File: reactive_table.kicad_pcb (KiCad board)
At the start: 4 copper layers, 111.8 x 116.8 mm, 184 parts, among them J1 BOT, J2 LEFT, J3 PROGRAM, J4 PWR_LEFT, J5 RIGHT, J6 PWR_RIGHT, J7 PWR_BOT, J8 TOP, J9 PWR_TOP, U1 uA7805, U2 CY8C4124PVI-432, U3 STP08DP05, U4 STP08DP05, U5 TLC274, U6 TLC274, U7 TLC274, U8 TLC274

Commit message: Reworked schematic. Started board
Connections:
- D23 pad 16: /LED Drivers & MUXs/IR15 -> /MUX_IN15
- D23 pad 17: /LED Drivers & MUXs/IR14 -> /MUX_IN14
- D23 pad 18: /LED Drivers & MUXs/IR13 -> /MUX_IN13
- D23 pad 19: /LED Drivers & MUXs/IR12 -> /MUX_IN12
- D23 pad 2: /LED Drivers & MUXs/IR7 -> /MUX_IN7
- D23 pad 20: /LED Drivers & MUXs/IR11 -> /MUX_IN11
- D23 pad 21: /LED Drivers & MUXs/IR10 -> /MUX_IN10
- D23 pad 22: /LED Drivers & MUXs/IR9 -> /MUX_IN9
- D23 pad 23: /LED Drivers & MUXs/IR8 -> /MUX_IN8
- D23 pad 3: /LED Drivers & MUXs/IR6 -> /MUX_IN6
- D23 pad 4: /LED Drivers & MUXs/IR5 -> /MUX_IN5
- D23 pad 5: /LED Drivers & MUXs/IR4 -> /MUX_IN4
- D23 pad 6: /LED Drivers & MUXs/IR3 -> /MUX_IN3
- D23 pad 7: /LED Drivers & MUXs/IR2 -> /MUX_IN2
- D23 pad 8: /LED Drivers & MUXs/IR1 -> /MUX_IN1
- D23 pad 9: /LED Drivers & MUXs/IR0 -> /MUX_IN0
- R1 pad 1: /Microcontroller/BOARD0 -> Net-(D23-Pad1)
- R1 pad 2: Net-(D23-Pad1) -> /Microcontroller/BOARD0
- R2 pad 1: GND -> /Microcontroller/BOARD0
- R2 pad 2: /Microcontroller/BOARD0 -> GND
- R51 pad 2: Net-(R51-Pad2) -> /LED Drivers & MUXs/IR0
- R52 pad 2: Net-(R52-Pad2) -> /LED Drivers & MUXs/IR1
- R53 pad 2: Net-(R53-Pad2) -> /LED Drivers & MUXs/IR2
- R54 pad 2: Net-(R54-Pad2) -> /LED Drivers & MUXs/IR3
- R55 pad 2: Net-(R55-Pad2) -> /LED Drivers & MUXs/IR4
- R56 pad 2: Net-(R56-Pad2) -> /LED Drivers & MUXs/IR5
- R57 pad 2: Net-(R57-Pad2) -> /LED Drivers & MUXs/IR6
- R58 pad 2: Net-(R58-Pad2) -> /LED Drivers & MUXs/IR7
- R59 pad 2: Net-(R59-Pad2) -> /LED Drivers & MUXs/IR8
- R60 pad 2: Net-(R60-Pad2) -> /LED Drivers & MUXs/IR9
- R61 pad 2: Net-(R61-Pad2) -> /LED Drivers & MUXs/IR10
- R62 pad 2: Net-(R62-Pad2) -> /LED Drivers & MUXs/IR11
- R63 pad 2: Net-(R63-Pad2) -> /LED Drivers & MUXs/IR12
- R64 pad 2: Net-(R64-Pad2) -> /LED Drivers & MUXs/IR13
- R65 pad 2: Net-(R65-Pad2) -> /LED Drivers & MUXs/IR14
- R66 pad 2: Net-(R66-Pad2) -> /LED Drivers & MUXs/IR15
- U5 pad 1: /LED Drivers & MUXs/IR0 -> /MUX_IN0
- U5 pad 10: Net-(R53-Pad2) -> /LED Drivers & MUXs/IR2
- U5 pad 12: Net-(R54-Pad2) -> /LED Drivers & MUXs/IR3
- U5 pad 13: /LED Drivers & MUXs/IR3 -> /MUX_IN3
- U5 pad 14: /LED Drivers & MUXs/IR3 -> /MUX_IN3
- U5 pad 2: /LED Drivers & MUXs/IR0 -> /MUX_IN0
- U5 pad 3: Net-(R51-Pad2) -> /LED Drivers & MUXs/IR0
- U5 pad 5: Net-(R52-Pad2) -> /LED Drivers & MUXs/IR1
- U5 pad 6: /LED Drivers & MUXs/IR1 -> /MUX_IN1
- U5 pad 7: /LED Drivers & MUXs/IR1 -> /MUX_IN1
- U5 pad 8: /LED Drivers & MUXs/IR2 -> /MUX_IN2
- U5 pad 9: /LED Drivers & MUXs/IR2 -> /MUX_IN2
- U6 pad 1: /LED Drivers & MUXs/IR4 -> /MUX_IN4
- U6 pad 10: Net-(R57-Pad2) -> /LED Drivers & MUXs/IR6
- U6 pad 12: Net-(R58-Pad2) -> /LED Drivers & MUXs/IR7
- U6 pad 13: /LED Drivers & MUXs/IR7 -> /MUX_IN7
- U6 pad 14: /LED Drivers & MUXs/IR7 -> /MUX_IN7
- U6 pad 2: /LED Drivers & MUXs/IR4 -> /MUX_IN4
- U6 pad 3: Net-(R55-Pad2) -> /LED Drivers & MUXs/IR4
- U6 pad 5: Net-(R56-Pad2) -> /LED Drivers & MUXs/IR5
- U6 pad 6: /LED Drivers & MUXs/IR5 -> /MUX_IN5
- U6 pad 7: /LED Drivers & MUXs/IR5 -> /MUX_IN5
- U6 pad 8: /LED Drivers & MUXs/IR6 -> /MUX_IN6
- U6 pad 9: /LED Drivers & MUXs/IR6 -> /MUX_IN6
- U7 pad 1: /LED Drivers & MUXs/IR8 -> /MUX_IN8
- U7 pad 10: Net-(R61-Pad2) -> /LED Drivers & MUXs/IR10
- U7 pad 12: Net-(R62-Pad2) -> /LED Drivers & MUXs/IR11
- U7 pad 13: /LED Drivers & MUXs/IR11 -> /MUX_IN11
- U7 pad 14: /LED Drivers & MUXs/IR11 -> /MUX_IN11
- U7 pad 2: /LED Drivers & MUXs/IR8 -> /MUX_IN8
- U7 pad 3: Net-(R59-Pad2) -> /LED Drivers & MUXs/IR8
- U7 pad 5: Net-(R60-Pad2) -> /LED Drivers & MUXs/IR9
- U7 pad 6: /LED Drivers & MUXs/IR9 -> /MUX_IN9
- U7 pad 7: /LED Drivers & MUXs/IR9 -> /MUX_IN9
- U7 pad 8: /LED Drivers & MUXs/IR10 -> /MUX_IN10
- U7 pad 9: /LED Drivers & MUXs/IR10 -> /MUX_IN10
- U8 pad 1: /LED Drivers & MUXs/IR12 -> /MUX_IN12
- U8 pad 10: Net-(R65-Pad2) -> /LED Drivers & MUXs/IR14
- U8 pad 12: Net-(R66-Pad2) -> /LED Drivers & MUXs/IR15
- U8 pad 13: /LED Drivers & MUXs/IR15 -> /MUX_IN15
- U8 pad 14: /LED Drivers & MUXs/IR15 -> /MUX_IN15
- U8 pad 2: /LED Drivers & MUXs/IR12 -> /MUX_IN12
- U8 pad 3: Net-(R63-Pad2) -> /LED Drivers & MUXs/IR12
- U8 pad 5: Net-(R64-Pad2) -> /LED Drivers & MUXs/IR13
- U8 pad 6: /LED Drivers & MUXs/IR13 -> /MUX_IN13
- U8 pad 7: /LED Drivers & MUXs/IR13 -> /MUX_IN13
- U8 pad 8: /LED Drivers & MUXs/IR14 -> /MUX_IN14
- U8 pad 9: /LED Drivers & MUXs/IR14 -> /MUX_IN14
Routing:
- net /BRD5: track 338.3 -> 0.00 mm, vias 1 -> 0
- net /BRD1: track 314.4 -> 0.00 mm, vias 1 -> 0
- net /BRD6: track 313.8 -> 0.00 mm, vias 1 -> 0
- net /CLK: track 307.0 -> 0.00 mm, vias 2 -> 0
- net /BRD2: track 305.7 -> 0.00 mm, vias 1 -> 0
- net /BRD3: track 302.3 -> 0.00 mm, vias 1 -> 0
- net /BRD4: track 299.3 -> 0.00 mm, vias 1 -> 0
- net /BRD7: track 282.7 -> 0.00 mm, vias 1 -> 0
- net /MUX3: track 250.6 -> 0.00 mm, vias 2 -> 0
- net /LE: track 239.8 -> 0.00 mm, vias 2 -> 0
- net /MUX1: track 236.1 -> 0.00 mm, vias 2 -> 0
- net /MUX2: track 221.6 -> 0.00 mm, vias 3 -> 0
- net /MUX0: track 218.1 -> 0.00 mm, vias 3 -> 0
- net /LED Drivers & MUXs/DRIVER_SDO: track 158.9 -> 0.00 mm, vias 2 -> 0
- net /SDI: track 152.9 -> 0.00 mm
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- removed copper zone on F.Cu, net +5V

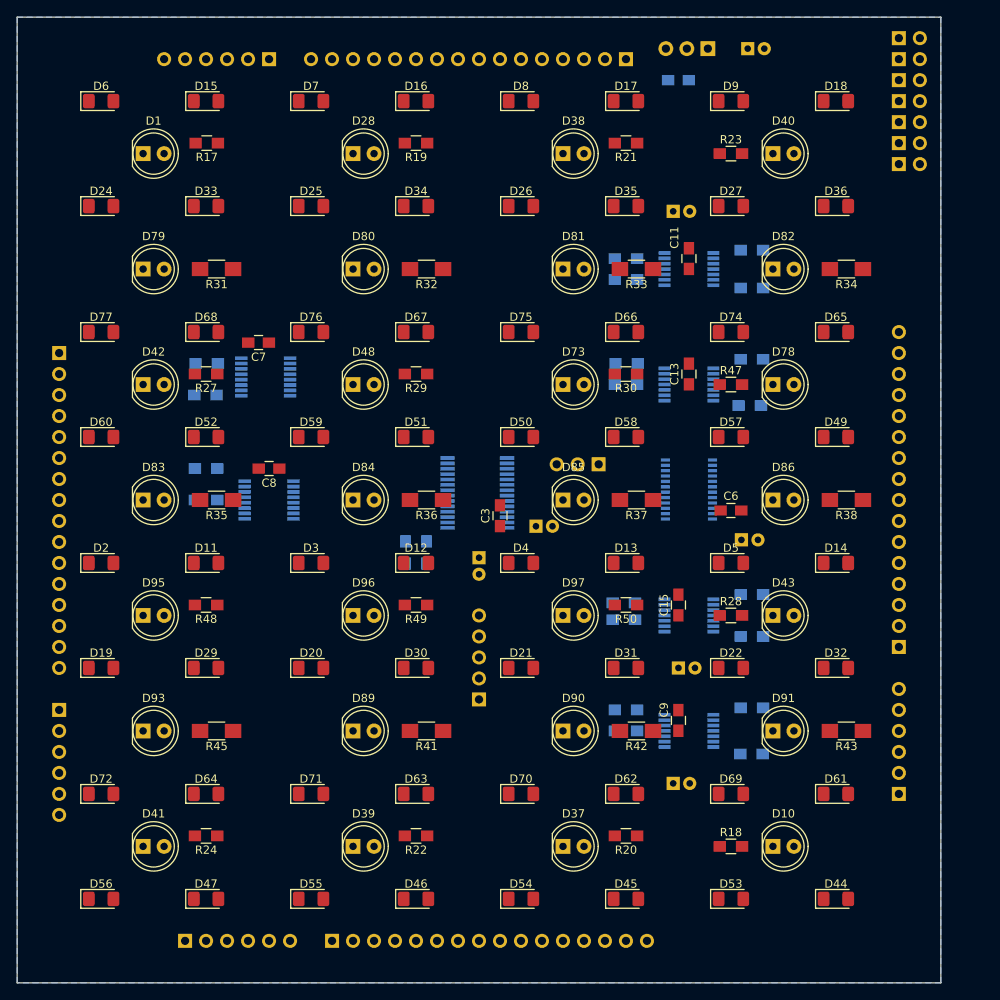
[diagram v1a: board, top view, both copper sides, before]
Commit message: Add main power connector for master board
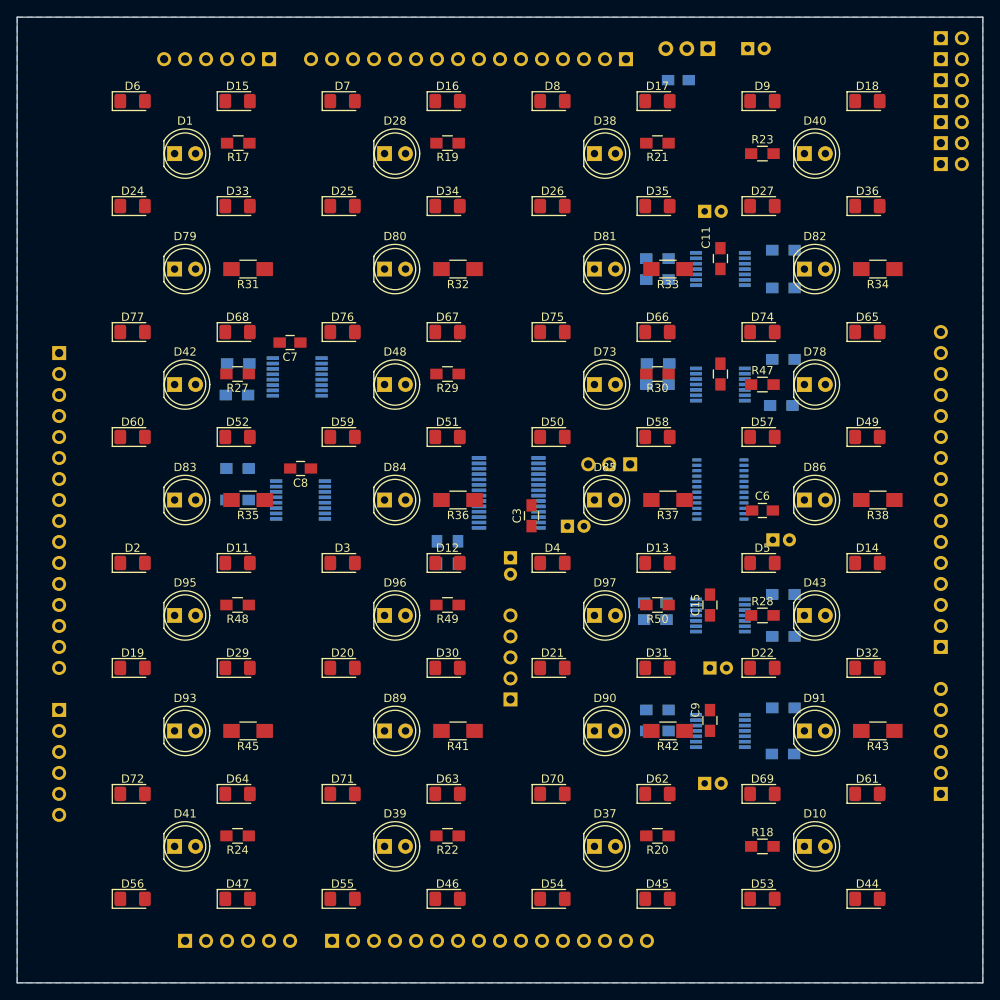
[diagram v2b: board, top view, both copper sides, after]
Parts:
- moved J5 5.08 mm to (166.4, 105.4)
- moved J6 5.08 mm to (166.4, 123.2)
- moved JP2 5.08 mm to (166.4, 47.0)
- moved JP3 5.08 mm to (166.4, 44.5)
- moved JP4 5.08 mm to (166.4, 41.9)
- moved JP5 5.08 mm to (166.4, 39.4)
- moved JP6 5.08 mm to (166.4, 36.8)
- moved JP7 5.08 mm to (166.4, 34.3)
- moved JP8 5.08 mm to (166.4, 31.8)
- moved C11 3.81 mm to (139.7, 58.4)
- moved C12 3.81 mm to (146.1, 92.5)
- moved C13 3.81 mm to (139.7, 72.4)
- moved C15 3.81 mm to (138.4, 100.3)
- moved C16 3.81 mm to (138.4, 108.0)
- moved C3 3.81 mm to (116.8, 89.5)
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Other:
- board size 111.8 x 116.8 mm -> 116.8 x 116.8 mm
